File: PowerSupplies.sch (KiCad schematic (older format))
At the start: 45 parts, among them Q301 BC847B-13-F, Q302 BC856B-13-F, Q305 TK32A12N1,S4X, Q306 TK32A12N1,S4X, U301 FDA217, U302 LTC7138EMSE-PBF, U303 TPS560200DBVR, U304 TLV70430DBVT, U305 REF2925AIDBZT, U306 TPS560200DBVR

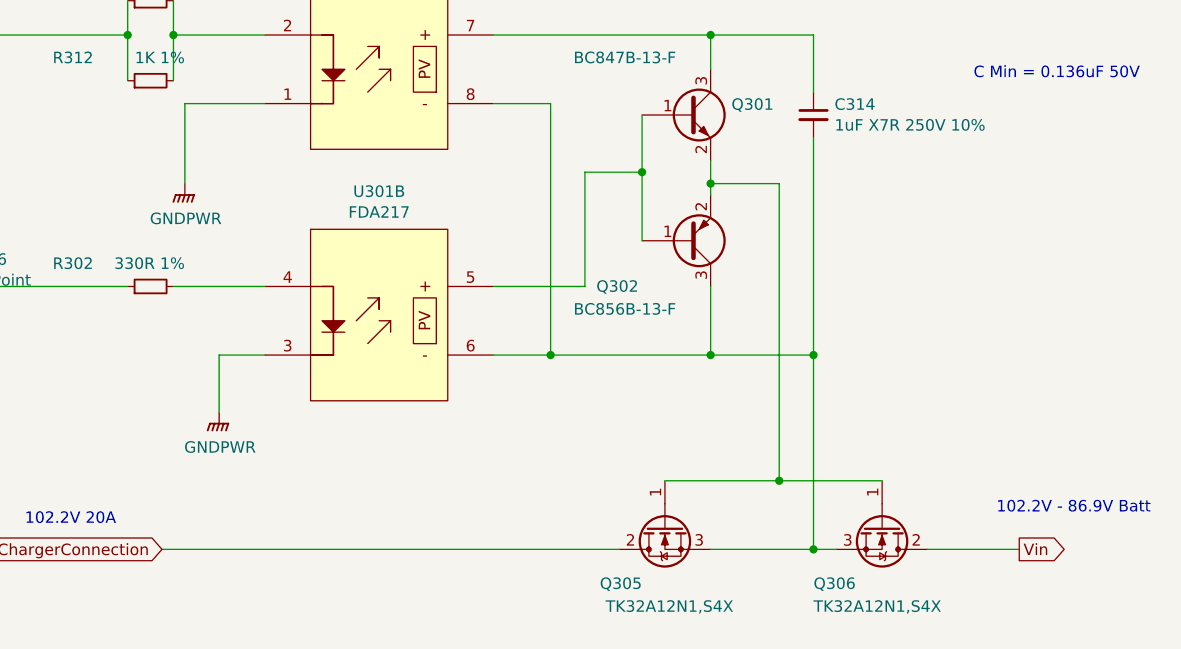
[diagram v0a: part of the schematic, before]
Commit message: Replaced TK32A12N1,S4X TO-220 Toshiba transistors that were use for turning the charger on and off, with a pair of IRFP4321PBF's from Infinion, in a TO-247AC package.  The reson for the change was this part of the circuit carries ~20A at 102.2V peak, so for a 30 degree rise in trace temp with 2 Once copper we need 5mm trace width, but we also need 1.1mm clearance, and this was differcult to acheive with the to-220 package, with out bending the legs etc. These devices are 2 time the price at about  with 15.5 mOhm vs 11 mOhm rds on.  Increased the main FETs gate drive trace to 2mm from 1mm.
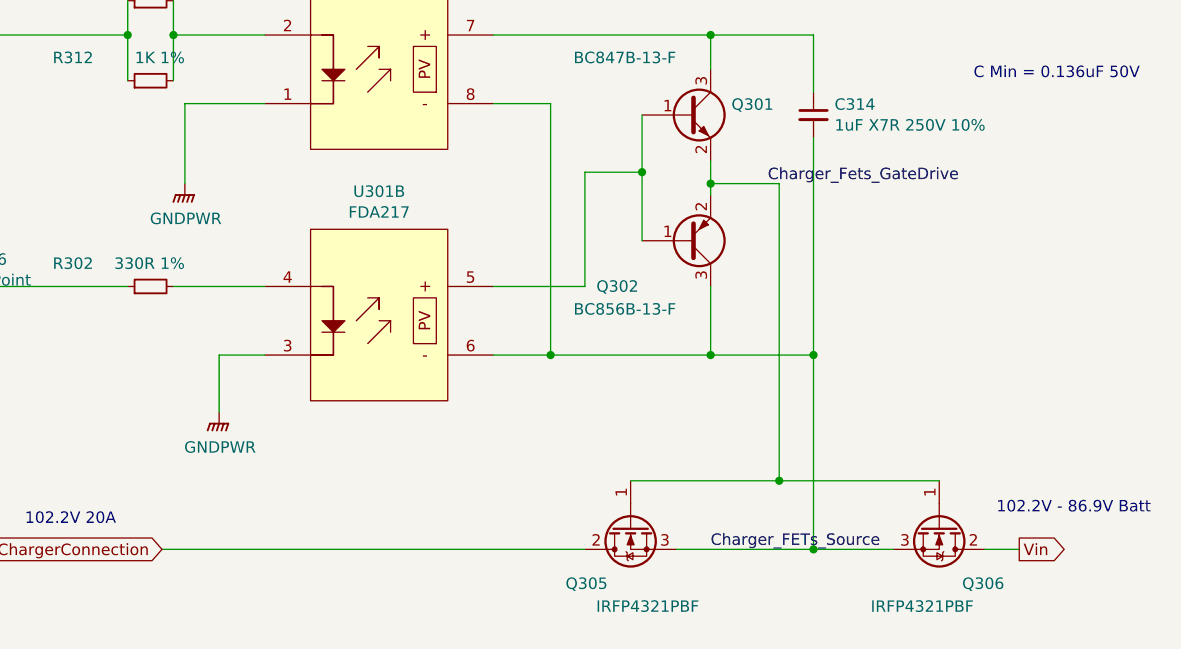
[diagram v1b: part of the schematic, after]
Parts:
- Q305, Q306: value TK32A12N1,S4X -> IRFP4321PBF; footprint Transistors_ThroughHole_jl:TO-220 -> Transistors_ThroughHole_jl:TO-247-3_Horizontal_TabDown; MFR Toshiba Semiconductor and Storage -> Infineon Technologies; MPN TK32A12N1,S4X -> IRFP4321PBF; SPN TK32A12N1S4X-ND -> IRFP4321PBF-ND
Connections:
- net Charger_Fets_GateDrive: now reaches Q301.2 (E), Q302.2 (E), Q305.1 (G), Q306.1 (G)
- net Charger_FETs_Source: now reaches C314.2, Q302.3 (C), Q305.3 (S), Q306.3 (S), U301.6, U301.8
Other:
- moved on the sheet: Q305
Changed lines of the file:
@@
-$Comp
-L Device:Q_NMOS_GDS Q?
-U 1 1 5ECCB06E
-P 9900 5750
-AR Path="/5ECCB06E" Ref="Q?"  Part="1"
-AR Path="/5EBD6442/5ECCB06E" Ref="Q306"  Part="1"
-F 0 "Q306" V 10150 5450 50  0000 L CNN
-F 1 "TK32A12N1,S4X" V 10250 5450 50  0000 L CNN
-F 2 "Transistors_ThroughHole_jl:TO-220" H 10100 5850 50  0001 C CNN
-F 3 "https://toshiba.semicon-storage.com/info/docget.jsp?did=13563&prodName=TK32A12N1" H 9900 5750 50  0001 C CNN
-F 4 "Toshiba Semiconductor and Storage" H 0   0   50  0001 C CNN "MFR"
-F 5 "TK32A12N1,S4X" H 0   0   50  0001 C CNN "MPN"
-F 6 "digikey" H 0   0   50  0001 C CNN "SPR"
-F 7 "TK32A12N1S4X-ND" H 0   0   50  0001 C CNN "SPN"
-F 8 "-" H 0   0   50  0001 C CNN "SPURL"
-	1    9900 5750
-	0    1    1    0
-$EndComp
 $Comp
 L Device:Q_NMOS_GDS Q?
 U 1 1 5ECCD1C3
-P 8950 5750
+P 8800 5750
 AR Path="/5ECCD1C3" Ref="Q?"  Part="1"
 AR Path="/5EBD6442/5ECCD1C3" Ref="Q305"  Part="1"
-F 0 "Q305" V 9200 5850 50  0000 L CNN
-F 1 "TK32A12N1,S4X" V 9300 5450 50  0000 L CNN
-F 2 "Transistors_ThroughHole_jl:TO-220" H 9150 5850 50  0001 C CNN
-F 3 "https://toshiba.semicon-storage.com/info/docget.jsp?did=13563&prodName=TK32A12N1" H 8950 5750 50  0001 C CNN
-F 4 "Toshiba Semiconductor and Storage" H 0   0   50  0001 C CNN "MFR"
-F 5 "TK32A12N1,S4X" H 0   0   50  0001 C CNN "MPN"
-F 6 "digikey" H 0   0   50  0001 C CNN "SPR"
-F 7 "TK32A12N1S4X-ND" H 0   0   50  0001 C CNN "SPN"
-F 8 "-" H 0   0   50  0001 C CNN "SPURL"
-	1    8950 5750
+F 0 "Q305" V 9050 5850 50  0000 L CNN
+F 1 "IRFP4321PBF" V 9150 5450 50  0000 L CNN
+F 2 "Transistors_ThroughHole_jl:TO-247-3_Horizontal_TabDown" H 9000 5850 50  0001 C CNN
+F 3 "https://www.infineon.com/dgdl/irfp4321pbf.pdf?fileId=5546d462533600a40153562c4f802011" H 8800 5750 50  0001 C CNN
+F 4 "Infineon Technologies" H -150 0   50  0001 C CNN "MFR"
+F 5 "IRFP4321PBF" H -150 0   50  0001 C CNN "MPN"
+F 6 "digikey" H -150 0   50  0001 C CNN "SPR"
+F 7 "IRFP4321PBF-ND" H -150 0   50  0001 C CNN "SPN"
+F 8 "-" H -150 0   50  0001 C CNN "SPURL"
+	1    8800 5750
 	0    -1   1    0
 $EndComp
@@
 	9500 900  9700 900
 Wire Wire Line
-	10100 5850 10500 5850
+	10350 5850 10500 5850
 Wire Wire Line
 	8200 3600 9150 3600
@@
 	9150 3750 9150 3600
 Wire Wire Line
-	9150 5850 9600 5850
+	9000 5850 9600 5850
 Wire Wire Line
 	9150 4150 9150 4250
 Wire Wire Line
-	8950 5550 9450 5550
+	8800 5550 9450 5550
 Wire Wire Line
 	9600 5000 9600 5850
 Wire Wire Line
-	9600 5850 9700 5850
+	9600 5850 9950 5850
 Wire Wire Line
 	9150 4250 9450 4250
@@
 	9150 4250 9150 4300
 Wire Wire Line
-	9450 5550 9900 5550
+	9450 5550 10150 5550
 Wire Wire Line
 	6800 4700 7200 4700
@@
 	2800 2550 3150 2550
 Wire Wire Line
-	6750 5850 8750 5850
+	6750 5850 8600 5850
 Wire Wire Line
 	9700 900  9850 900
@@
 Connection ~ 3950 3000
 Connection ~ 3950 2250
+$Comp
+L Device:Q_NMOS_GDS Q?
+U 1 1 5F305B10
+P 10150 5750
+AR Path="/5F305B10" Ref="Q?"  Part="1"
+AR Path="/5EBD6442/5F305B10" Ref="Q306"  Part="1"
+F 0 "Q306" V 10400 5850 50  0000 L CNN
+F 1 "IRFP4321PBF" V 10500 5450 50  0000 L CNN
+F 2 "Transistors_ThroughHole_jl:TO-247-3_Horizontal_TabDown" H 10350 5850 50  0001 C CNN
+F 3 "https://www.infineon.com/dgdl/irfp4321pbf.pdf?fileId=5546d462533600a40153562c4f802011" H 10150 5750 50  0001 C CNN
+F 4 "Infineon Technologies" H 1200 0   50  0001 C CNN "MFR"
+F 5 "IRFP4321PBF" H 1200 0   50  0001 C CNN "MPN"
+F 6 "digikey" H 1200 0   50  0001 C CNN "SPR"
+F 7 "IRFP4321PBF-ND" H 1200 0   50  0001 C CNN "SPN"
+F 8 "-" H 1200 0   50  0001 C CNN "SPURL"
+	1    10150 5750
+	0    1    1    0
+$EndComp
+Text Label 9400 4250 0    50   ~ 0
+Charger_Fets_GateDrive
+Text Label 9150 5850 0    50   ~ 0
+Charger_FETs_Source
 $EndSCHEMATC

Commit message: Found that my local updates of Kicad footprint librarys, had changed the names of resistor and capacitor footprints, so I updated all these footprint names.  Added circuit to measure the Vin via pin 28 of the Teensy-LC, This will allow the battery system to shut down if the battery voltage gets too low.
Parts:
- C301, C305, C307, C308, C310, C311: footprint Capacitors_SMD:C_1206_HandSoldering -> Capacitor_SMD:C_1206_3216Metric_Pad1.42x1.75mm_HandSolder
- C302, C304, C309, C312, C313: footprint Capacitors_SMD:C_0805_HandSoldering -> Capacitor_SMD:C_0805_2012Metric_Pad1.15x1.40mm_HandSolder
- C303, C314: footprint Capacitors_SMD:C_2220_HandSoldering -> Capacitor_SMD:C_2220_5650Metric_Pad1.97x5.40mm_HandSolder
- C306, C315: footprint Capacitors_SMD:C_1812_HandSoldering -> Capacitor_SMD:C_1812_4532Metric_Pad1.30x3.40mm_HandSolder
- D301: footprint Diodes_SMD:D_SMA_Handsoldering -> Diode_SMD:D_SMA_Handsoldering
- R301, R302, R303, R304, R308, R309, R310, R311, R312: footprint Resistors_SMD:R_0805_HandSoldering -> Resistor_SMD:R_0805_2012Metric_Pad1.15x1.40mm_HandSolder

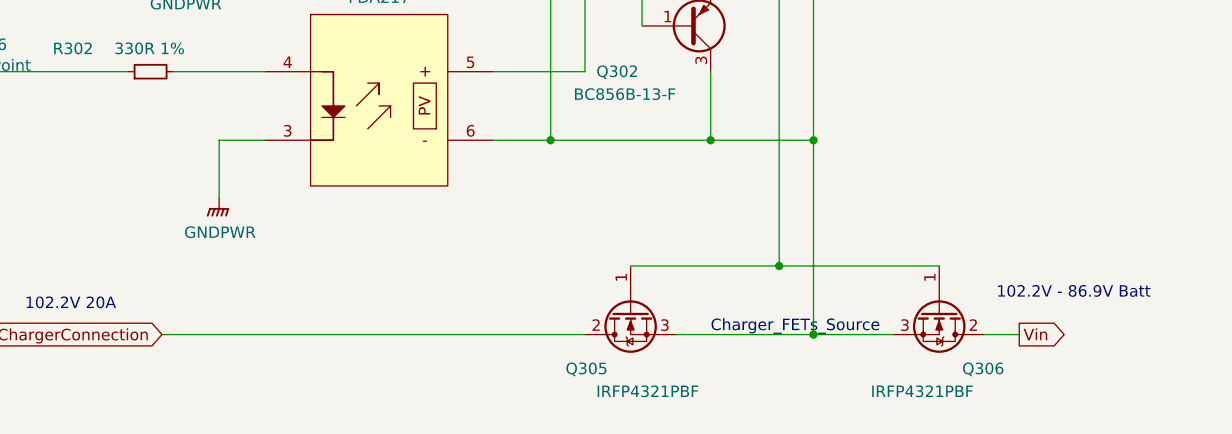
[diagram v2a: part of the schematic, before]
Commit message: Added a dedicated fuse for the charger connection.  Lowered the fuses from 25A to 20A after looking more closely at the data sheet.  Charger is 19.5A atmost and Battery current draw at 80% efficency, 86.8V, 1000W is 14.4A. Reduced the voltage divider resistance for the MainPowerMonitor from 2x 10K to 2x 1K, the reason for this is to draw 1.25mA from the 3.0V supply to increase its effectiveness as input protection for the micro inputs, the BAT54S diodes connect to the 3.0V power supplys so will conduct to this if the input risees a diode drop above 3.0V, so the more current draw from this supply the more it can sink without rising.
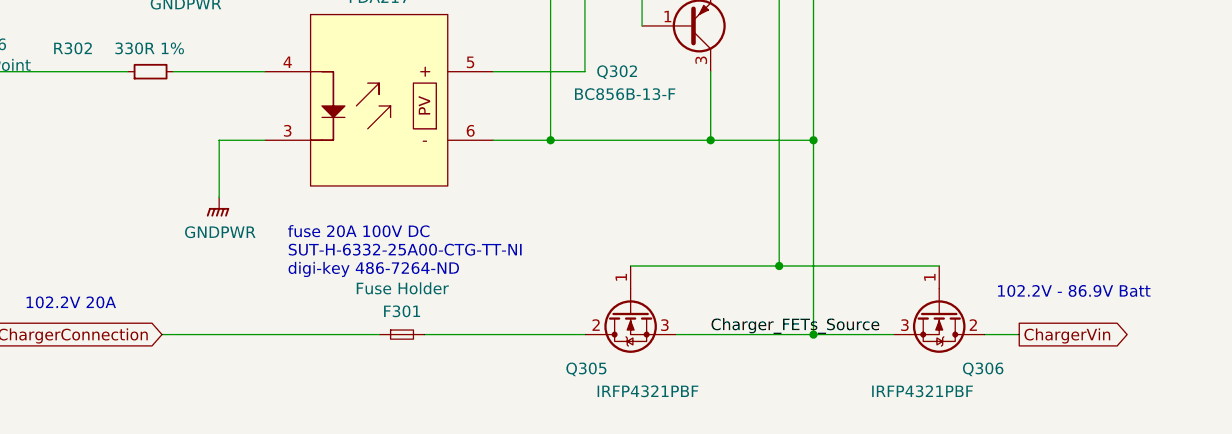
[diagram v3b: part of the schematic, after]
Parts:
- added F301: Fuse Holder, Connect_jl:BellFuse_6.3mmX32mm_FC_102-22, symbol Device:Fuse_Small
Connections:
- net ChargerConnection: now also F301.1; no longer Q305.2 (D)
- net Vin: no longer Q306.2 (D)
- new net: F301.2, Q305.2 (D)
- new net ChargerVin: Q306.2 (D)
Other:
- note added: "fuse 20A 100V DC\nSUT-H-6332-25A00-CTG-TT-NI\ndigi-key 486-7264-ND"
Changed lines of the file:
@@
 	1    0    0    -1
+$EndComp
+$Comp
+L Device:Q_NMOS_GDS Q?
+U 1 1 5F305B10
+P 10150 5750
+AR Path="/5F305B10" Ref="Q?"  Part="1"
+AR Path="/5EBD6442/5F305B10" Ref="Q306"  Part="1"
+F 0 "Q306" V 10400 5850 50  0000 L CNN
+F 1 "IRFP4321PBF" V 10500 5450 50  0000 L CNN
+F 2 "Transistors_ThroughHole_jl:TO-247-3_Horizontal_TabDown" H 10350 5850 50  0001 C CNN
+F 3 "https://www.infineon.com/dgdl/irfp4321pbf.pdf?fileId=5546d462533600a40153562c4f802011" H 10150 5750 50  0001 C CNN
+F 4 "Infineon Technologies" H 1200 0   50  0001 C CNN "MFR"
+F 5 "IRFP4321PBF" H 1200 0   50  0001 C CNN "MPN"
+F 6 "digikey" H 1200 0   50  0001 C CNN "SPR"
+F 7 "IRFP4321PBF-ND" H 1200 0   50  0001 C CNN "SPN"
+F 8 "-" H 1200 0   50  0001 C CNN "SPURL"
+	1    10150 5750
+	0    1    1    0
 $EndComp
 Text GLabel 3450 2550 2    50   Input ~ 0
@@
 +3.0V
 Text GLabel 10500 5850 2    50   Output ~ 0
-Vin
+ChargerVin
 Text Notes 10300 3800 0    50   ~ 0
 C Min = 0.136uF 50V
@@
 Text Notes 4900 2850 0    50   ~ 0
 Need about 30uF for 1% ripple, but part has\n20% tolerance and down 35% with 11V\nDC bias.
+Text Label 9400 4250 0    50   ~ 0
+Charger_Fets_GateDrive
+Text Label 9150 5850 0    50   ~ 0
+Charger_FETs_Source
 Wire Wire Line
 	1000 2150 700  2150
@@
 Wire Wire Line
 	2800 2550 3150 2550
-Wire Wire Line
-	6750 5850 8600 5850
 Wire Wire Line
 	9700 900  9850 900
@@
 Connection ~ 3950 2250
 $Comp
-L Device:Q_NMOS_GDS Q?
-U 1 1 5F305B10
-P 10150 5750
-AR Path="/5F305B10" Ref="Q?"  Part="1"
-AR Path="/5EBD6442/5F305B10" Ref="Q306"  Part="1"
-F 0 "Q306" V 10400 5850 50  0000 L CNN
-F 1 "IRFP4321PBF" V 10500 5450 50  0000 L CNN
-F 2 "Transistors_ThroughHole_jl:TO-247-3_Horizontal_TabDown" H 10350 5850 50  0001 C CNN
-F 3 "https://www.infineon.com/dgdl/irfp4321pbf.pdf?fileId=5546d462533600a40153562c4f802011" H 10150 5750 50  0001 C CNN
-F 4 "Infineon Technologies" H 1200 0   50  0001 C CNN "MFR"
-F 5 "IRFP4321PBF" H 1200 0   50  0001 C CNN "MPN"
-F 6 "digikey" H 1200 0   50  0001 C CNN "SPR"
-F 7 "IRFP4321PBF-ND" H 1200 0   50  0001 C CNN "SPN"
-F 8 "-" H 1200 0   50  0001 C CNN "SPURL"
-	1    10150 5750
-	0    1    1    0
+L Device:Fuse_Small F?
+U 1 1 5F75F007
+P 7800 5850
+AR Path="/5F75F007" Ref="F?"  Part="1"
+AR Path="/5EBD6442/5F75F007" Ref="F301"  Part="1"
+F 0 "F301" H 7800 5950 50  0000 C CNN
+F 1 "Fuse Holder" H 7800 6050 50  0000 C CNN
+F 2 "Connect_jl:BellFuse_6.3mmX32mm_FC_102-22" H 7850 5650 50  0001 L CNN
+F 3 "https://us.schurter.com/en/datasheet/typ_SUT-H_6.3x32.pdf" H 7800 5850 50  0001 C CNN
+F 4 "https://belfuse.com/resources/datasheets/circuitprotection/ds-cp-0672-fuse-clips-series.pdf" H 7800 5850 50  0001 C CNN "Holder DataSheet"
+F 5 "Bel Fuse Inc." H 5800 4150 50  0001 C CNN "MFR"
+F 6 "FC-102-22" H 5800 4150 50  0001 C CNN "MPN"
+F 7 "digikey" H 5800 4150 50  0001 C CNN "SPR"
+F 8 "507-1702-ND" H 5800 4150 50  0001 C CNN "SPN"
+F 9 "-" H 5800 4150 50  0001 C CNN "SPURL"
+	1    7800 5850
+	1    0    0    -1
 $EndComp
-Text Label 9400 4250 0    50   ~ 0
-Charger_Fets_GateDrive
-Text Label 9150 5850 0    50   ~ 0
-Charger_FETs_Source
+Text Notes 7300 5600 0    50   ~ 0
+fuse 20A 100V DC\nSUT-H-6332-25A00-CTG-TT-NI\ndigi-key 486-7264-ND
+Wire Wire Line
+	7900 5850 8600 5850
+Wire Wire Line
+	6750 5850 7700 5850
 $EndSCHEMATC

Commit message: Added voltage divider network and input protection to measure, the Solar input voltage, I decided this would be usefull in the cases where the solar is producing voltage over 160V, but the house is stillimporting power from the Grid, there is not point in powering up the boost converter because we can't get power into the system, as output is 160V.  Also update the TestPoint footprints to match the latest Kicad naming convention, simular to my resistor and capacitor footprint changes a few commits ago.
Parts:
- TP301, TP303, TP304, TP305, TP306, TP307: footprint Measurement_Points:Measurement_Point_Square-SMD-Pad_Big -> TestPoint:TestPoint_Pad_3.0x3.0mm
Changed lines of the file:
@@
 F 0 "TP304" H 4308 1068 50  0000 L CNN
 F 1 "TestPoint" H 4308 977 50  0000 L CNN
-F 2 "Measurement_Points:Measurement_Point_Square-SMD-Pad_Big" H 4450 950 50  0001 C CNN
+F 2 "TestPoint:TestPoint_Pad_3.0x3.0mm" H 4450 950 50  0001 C CNN
 F 3 "~" H 4450 950 50  0001 C CNN
 F 4 "-" H 0   0   50  0001 C CNN "MFR"
@@
 F 0 "TP303" V 4154 1738 50  0000 L CNN
 F 1 "TestPoint" V 4245 1738 50  0000 L CNN
-F 2 "Measurement_Points:Measurement_Point_Square-SMD-Pad_Big" H 4400 1550 50  0001 C CNN
+F 2 "TestPoint:TestPoint_Pad_3.0x3.0mm" H 4400 1550 50  0001 C CNN
 F 3 "~" H 4400 1550 50  0001 C CNN
 F 4 "-" H 0   0   50  0001 C CNN "MFR"
@@
 F 0 "TP301" V 3754 4238 50  0000 L CNN
 F 1 "TestPoint" V 3845 4238 50  0000 L CNN
-F 2 "Measurement_Points:Measurement_Point_Square-SMD-Pad_Big" H 4000 4050 50  0001 C CNN
+F 2 "TestPoint:TestPoint_Pad_3.0x3.0mm" H 4000 4050 50  0001 C CNN
 F 3 "~" H 4000 4050 50  0001 C CNN
 F 4 "-" H 0   0   50  0001 C CNN "MFR"
@@
 F 0 "TP305" H 4358 6018 50  0000 L CNN
 F 1 "TestPoint" H 4358 5927 50  0000 L CNN
-F 2 "Measurement_Points:Measurement_Point_Square-SMD-Pad_Big" H 4500 5900 50  0001 C CNN
+F 2 "TestPoint:TestPoint_Pad_3.0x3.0mm" H 4500 5900 50  0001 C CNN
 F 3 "~" H 4500 5900 50  0001 C CNN
 F 4 "-" H 0   0   50  0001 C CNN "MFR"
@@
 F 0 "TP307" H 10708 1018 50  0000 L CNN
 F 1 "TestPoint" H 10708 927 50  0000 L CNN
-F 2 "Measurement_Points:Measurement_Point_Square-SMD-Pad_Big" H 10850 900 50  0001 C CNN
+F 2 "TestPoint:TestPoint_Pad_3.0x3.0mm" H 10850 900 50  0001 C CNN
 F 3 "~" H 10850 900 50  0001 C CNN
 F 4 "-" H 0   0   50  0001 C CNN "MFR"
@@
 F 0 "TP306" H 5858 4818 50  0000 L CNN
 F 1 "TestPoint" H 5858 4727 50  0000 L CNN
-F 2 "Measurement_Points:Measurement_Point_Square-SMD-Pad_Big" H 6000 4700 50  0001 C CNN
+F 2 "TestPoint:TestPoint_Pad_3.0x3.0mm" H 6000 4700 50  0001 C CNN
 F 3 "~" H 6000 4700 50  0001 C CNN
 F 4 "-" H 0   0   50  0001 C CNN "MFR"

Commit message: Regenerated BOM after adding Solar Voltage measuring circuit, and updated TestPoint footprint that was missed in earler commit.
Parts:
- TP302: footprint Measurement_Points:Measurement_Point_Square-SMD-Pad_Big -> TestPoint:TestPoint_Pad_3.0x3.0mm
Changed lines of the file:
@@
 F 0 "TP302" H 4008 3818 50  0000 L CNN
 F 1 "TestPoint" H 4008 3727 50  0000 L CNN
-F 2 "Measurement_Points:Measurement_Point_Square-SMD-Pad_Big" H 4150 3700 50  0001 C CNN
+F 2 "TestPoint:TestPoint_Pad_3.0x3.0mm" H 4150 3700 50  0001 C CNN
 F 3 "~" H 4150 3700 50  0001 C CNN
 F 4 "-" H 0   0   50  0001 C CNN "MFR"
